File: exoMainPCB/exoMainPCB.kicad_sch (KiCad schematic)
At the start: 91 parts, among them J1 Conn_02x06_Odd_Even, J10 Conn_01x03_Pin, J11 USB_A, J12 USB_A, J13 USB_A, J14 Screw_Terminal_01x02, J2 HDMI_A, J3 USB_A, J4 Conn_01x02, J5 Conn_01x03, J6 Conn_01x03_Pin, J7 Conn_01x02, J8 Screw_Terminal_01x02, SW1 SW_SPDT, SW2 SW_Push, SW3 SW_SPDT, U1 MCP2515-I/ST, U14 SI8642ED-B-IS, U15 SN65HVD230D, U17 SM24CANB-02HTG, U2 MCP2515-I/ST, U3 BNO085, U4 SL2.1A, U5 MCP3008, U7 SN65HVD230D, U8 SM24CANB-02HTG, Y1 16 MHz, Y2 16 MHz, Y3 12 MHz, Y4 32.768 kHz

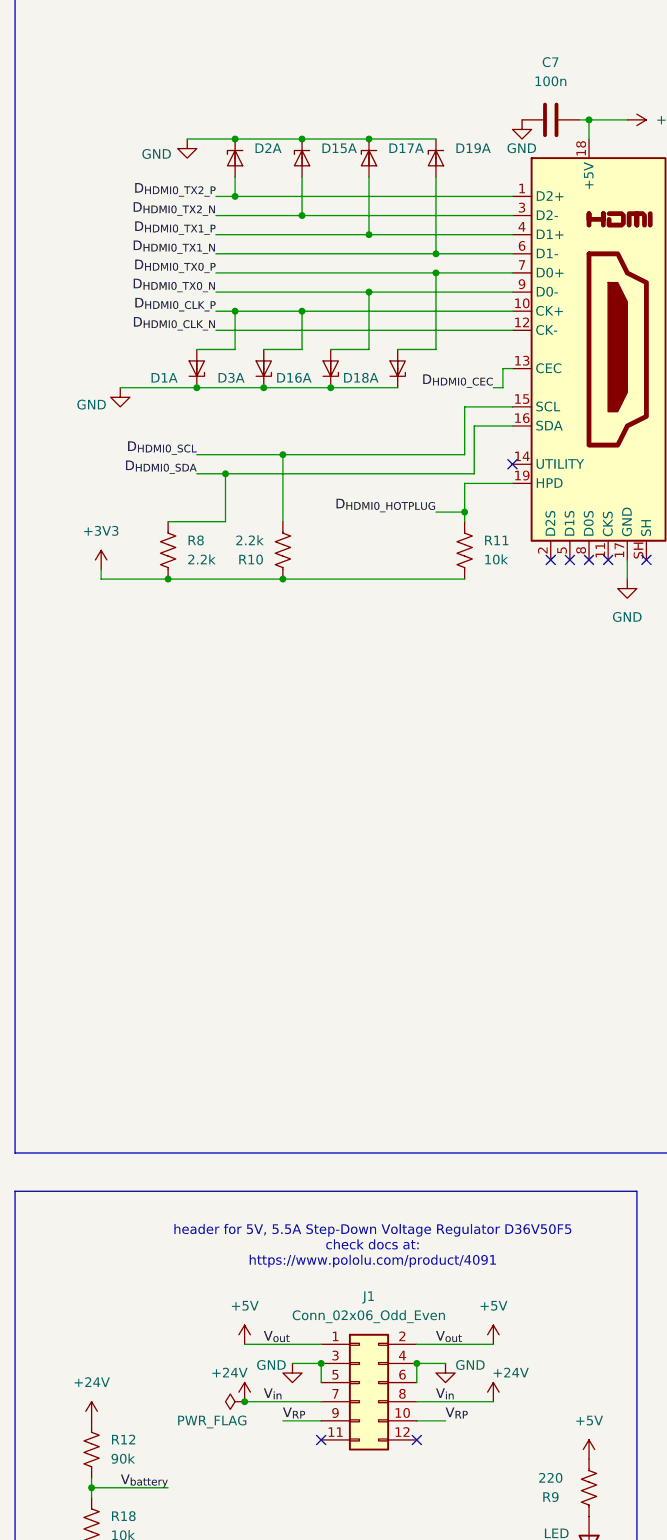
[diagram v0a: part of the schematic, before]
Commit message: fixed TVS diodes on HDMI, changed Vin and Vout to text rather than labels
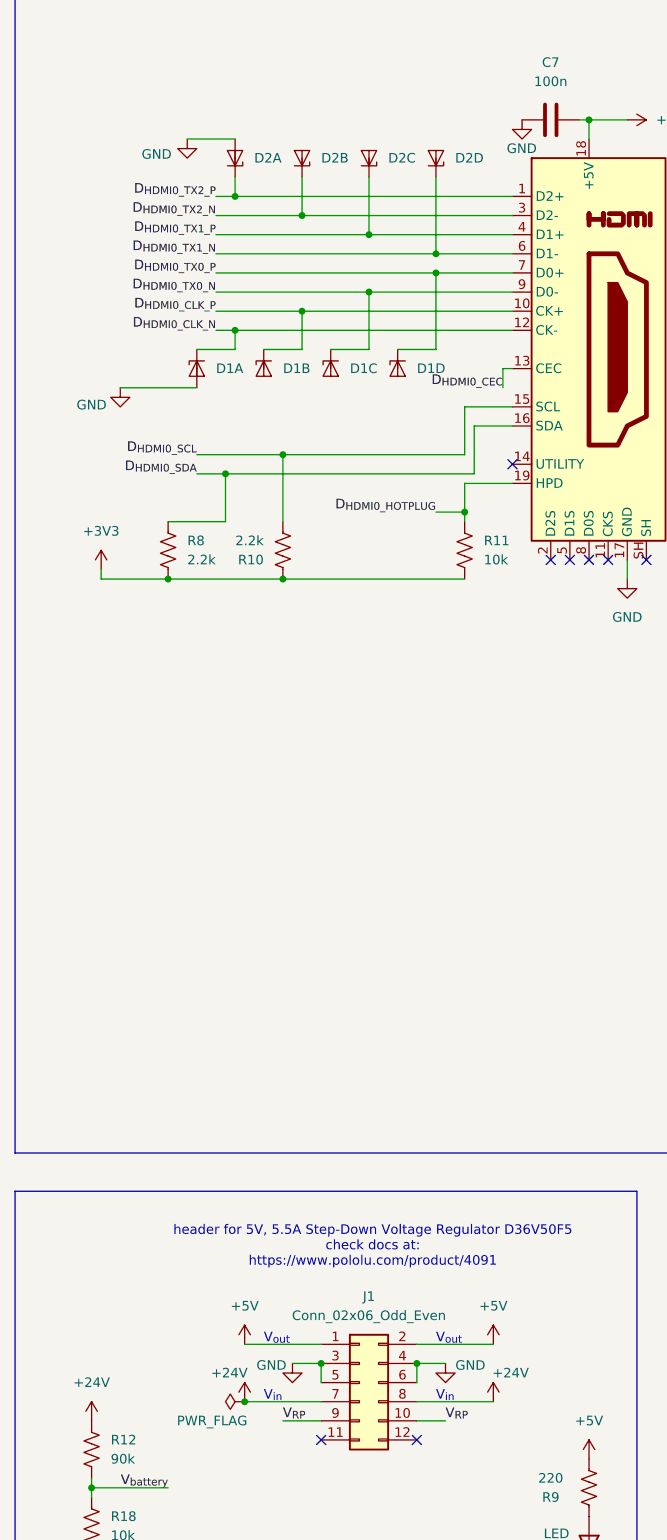
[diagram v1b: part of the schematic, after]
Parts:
- renumbered D18 to D1, D3 to D1, D16 to D1, D19 to D2, D15 to D2, D17 to D2
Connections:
- net D_{HDMI0_CLK_N}: now also D1.1 (K1)
- net D_{HDMI0_CLK_P}: now also D1.3 (K2); no longer D1.2 (A), D1.2 (A), D1.5 (A), D1.5 (A)
- net D_{HDMI0_TX0_N}: now also D1.4 (K3); no longer D1.2 (A), D1.5 (A)
- net D_{HDMI0_TX0_P}: now also D1.6 (K4); no longer D1.2 (A), D1.5 (A)
- net D_{HDMI0_TX1_N}: now also D2.6 (K4); no longer D2.2 (A), D2.5 (A)
- net D_{HDMI0_TX1_P}: now also D2.4 (K3); no longer D2.2 (A), D2.5 (A)
- net D_{HDMI0_TX2_N}: now also D2.3 (K2); no longer D2.2 (A), D2.5 (A)
- net D_{HDMI0_TX2_P}: now also D2.1 (K1); no longer D2.2 (A), D2.5 (A)
- net GND: now also D1.2 (A), D1.5 (A), D2.2 (A), D2.5 (A); no longer D1.1 (K1), D1.1 (K1), D1.1 (K1), D1.1 (K1), D2.1 (K1), D2.1 (K1), D2.1 (K1), D2.1 (K1)
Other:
- note added: "V_{in}"
- note added: "V_{out}"
- moved on the sheet: D1A, D2A

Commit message: assigned all footprints, created new footprints based on part availability
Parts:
- added C18, C20, C21, C22: 47uF, Capacitor_SMD:C_0805_2012Metric, symbol Device:C
- added J15: Conn_01x03, Connector_PinSocket_2.54mm:PinSocket_1x03_P2.54mm_Vertical, symbol Connector_Generic:Conn_01x03
- added J16: Conn_01x02, Connector_PinSocket_2.54mm:PinSocket_1x02_P2.54mm_Vertical, symbol Connector_Generic:Conn_01x02
- added J9: Conn_01x12, Connector_PinSocket_2.54mm:PinSocket_1x12_P2.54mm_Vertical, symbol Connector_Generic:Conn_01x12
- C1, C10, C11, C12, C15, C16, C17, C19, C2, C3, C33, C35, C4, C5, C6, C7: footprint (none) -> Capacitor_SMD:C_0805_2012Metric
- C13, C14, C8, C9: value 100uF -> 47uF; footprint (none) -> Capacitor_SMD:C_0805_2012Metric
- J1: footprint (none) -> Connector_PinSocket_2.54mm:PinSocket_2x06_P2.54mm_Vertical
- J10, J6: footprint (none) -> Connector_PinHeader_2.54mm:PinHeader_1x03_P2.54mm_Vertical
- J11, J12, J13, J3: footprint (none) -> BNO085:USB C2345
- J14, J8: footprint (none) -> BNO085:1x2 Screw Terminal C3703
- J2: footprint (none) -> Connector_Video:HDMI_A_Molex_208658-1001_Horizontal
- J4, J7: footprint (none) -> Connector_PinSocket_2.54mm:PinSocket_1x02_P2.54mm_Vertical
- J5: footprint (none) -> Connector_PinSocket_2.54mm:PinSocket_1x03_P2.54mm_Vertical
- JP1, JP2, JP7, JP8: footprint (none) -> Jumper:SolderJumper-2_P1.3mm_Open_RoundedPad1.0x1.5mm
- JP3, JP4, JP5, JP6, JP9: footprint (none) -> Jumper:SolderJumper-2_P1.3mm_Bridged_RoundedPad1.0x1.5mm
- R1, R10, R11, R12, R17, R18, R2, R3, R4, R5, R6, R7, R8: footprint (none) -> Resistor_SMD:R_0805_2012Metric
- R13, R14, R15, R16, R26, R9: footprint (none) -> Resistor_SMD:R_1206_3216Metric
- SW1, SW3: footprint (none) -> BNO085:ALPSALPINE C125042
- SW2: footprint (none) -> BNO085:SPEH SMD Pushbutton
- U1, U2: footprint SOP65P640X120-20N -> MCP2515-IST:SOP65P640X120-20N
- U14: footprint SOIC127P1030X265-16N -> SI8642ED-B-IS:SOIC127P1030X265-16N
- U15, U7: footprint SOIC127P600X175-8N -> SN65HVD230:SOIC127P600X175-8N
- U17, U8: footprint SM24CANB02HTG -> SM24CANB:SM24CANB02HTG
- U4: footprint my_lib:SOP-16_L10.0-W3.9-P1.27-LS6.0-BL -> Package_SO:SOP-16_3.9x9.9mm_P1.27mm
- U5: footprint (none) -> Package_SO:SOIC-16_3.9x9.9mm_P1.27mm
- Y1, Y2, Y3, Y4: footprint (none) -> Crystal:Crystal_SMD_2520-4Pin_2.5x2.0mm
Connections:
- net +5V: now also C18.1, C20.1, C21.1, C22.1
- net GND: now also C18.2, C20.2, C21.2, C22.2, J9.1 (Pin_1)
- net MISO: now also J15.2 (Pin_2)
- net MOSI: now also J15.1 (Pin_1)
- net SCK: now also J15.3 (Pin_3)
- net SCL: now also J16.2 (Pin_2)
- net SDA: now also J16.1 (Pin_1)
- net GPIO21: now reaches Module1.25 (GPIO21)
- net GPIO21: now also J9.12 (Pin_12)
- net GPIO20: now reaches Module1.27 (GPIO20)
- net GPIO20: now also J9.11 (Pin_11)
- net GPIO16: now reaches Module1.29 (GPIO16)
- net GPIO16: now also J9.10 (Pin_10)
- net GPIO12: now reaches Module1.31 (GPIO12)
- net GPIO12: now also J9.9 (Pin_9)
- net GPIO24: now reaches Module1.45 (GPIO24)
- net GPIO24: now also J9.8 (Pin_8)
- net GPIO23: now reaches Module1.47 (GPIO23)
- net GPIO23: now also J9.7 (Pin_7)
- net GPIO18: now reaches Module1.49 (GPIO18)
- net GPIO18: now also J9.6 (Pin_6)
- net GPIO15: now reaches Module1.51 (GPIO15)
- net GPIO15: now also J9.5 (Pin_5)
- net GPIO4: now reaches Module1.54 (GPIO4)
- net GPIO4: now also J9.3 (Pin_3)
- net GPIO14: now reaches Module1.55 (GPIO14)
- net GPIO14: now also J9.4 (Pin_4)
- new net +3.3V: J9.2 (Pin_2)
- no-connect marks 144 -> 134
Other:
- note added: "Extra Connection Pins for Future Modification"
- moved on the sheet: C13, C14, C8, C9

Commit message: pcb layout complete
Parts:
- removed JP6: SolderJumper_2_Bridged, Jumper:SolderJumper-2_P1.3mm_Bridged_RoundedPad1.0x1.5mm, symbol Jumper:SolderJumper_2_Bridged
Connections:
- net +24V: no longer J5.2 (Pin_2)
- net +3V3: no longer C16.2, U4.13 (VDD33)
- net +5V: now also Module1.77 (+5v_(Input)), Module1.79 (+5v_(Input)), Module1.81 (+5v_(Input)), Module1.83 (+5v_(Input)), Module1.85 (+5v_(Input)), Module1.87 (+5v_(Input))
- net D_{HDMI0_CLK_N}: now also D1.6 (K4); no longer D1.1 (K1)
- net D_{HDMI0_CLK_P}: now also D1.4 (K3); no longer D1.3 (K2)
- net D_{HDMI0_TX0_N}: now also D1.3 (K2); no longer D1.4 (K3)
- net D_{HDMI0_TX0_P}: now also D1.1 (K1); no longer D1.6 (K4)
- net V_{RP}: now also J5.2 (Pin_2)
- net +1V8: no longer names the net of C15.2, U4.14 (VDD18)
- net +1V8: no longer Module1.88 (+1.8v_(Output))
- new net: C16.2, U4.13 (VDD33)
- no-connect marks 134 -> 135

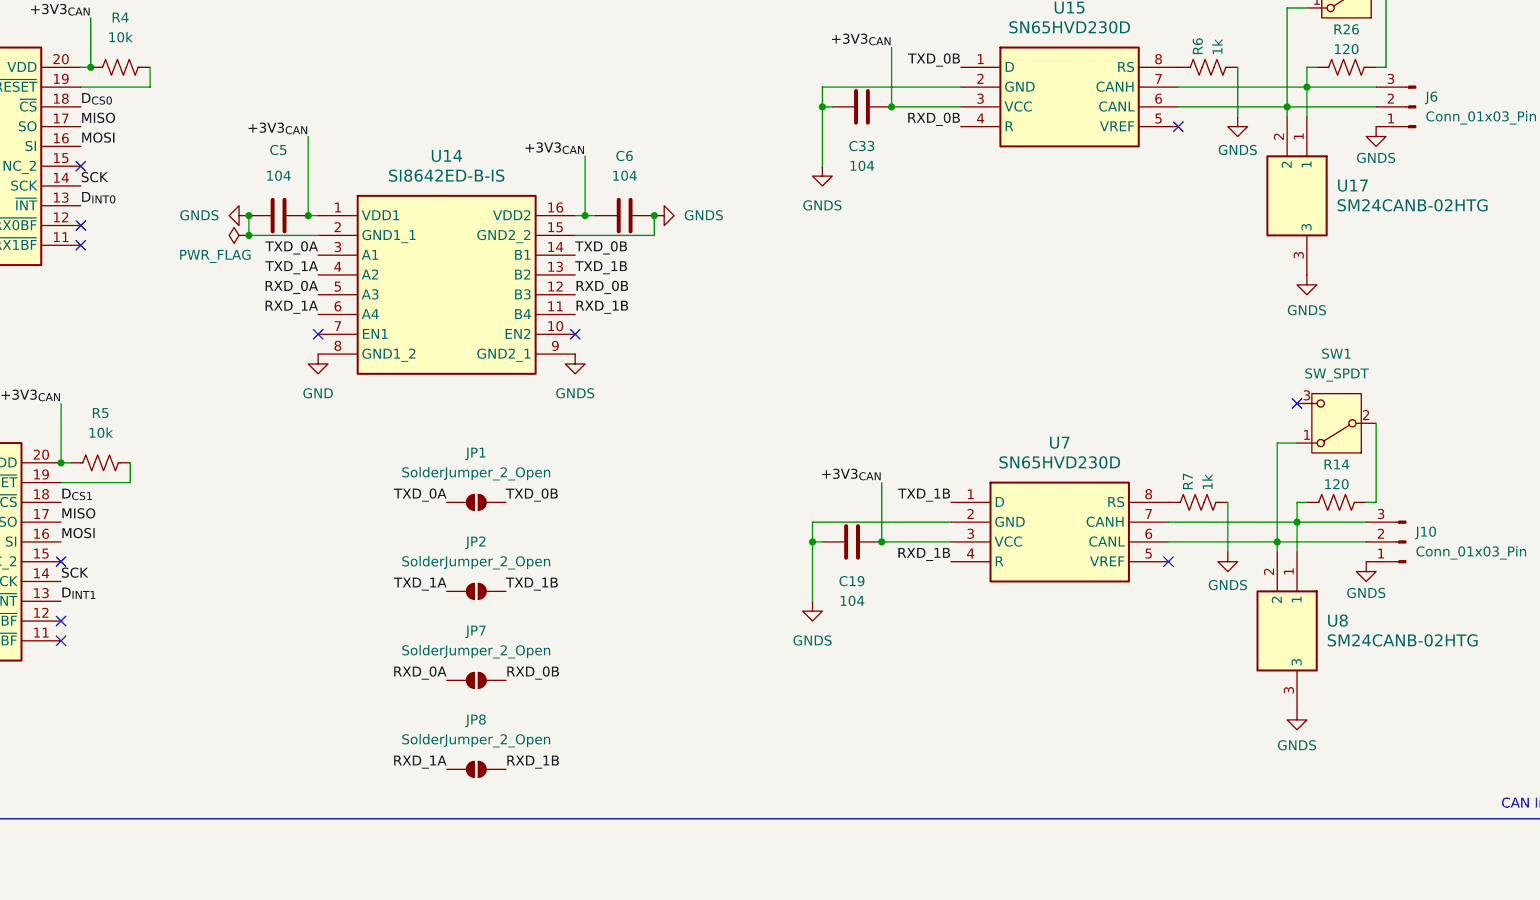
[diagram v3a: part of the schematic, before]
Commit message: added silkscreen labels, completed ground pours
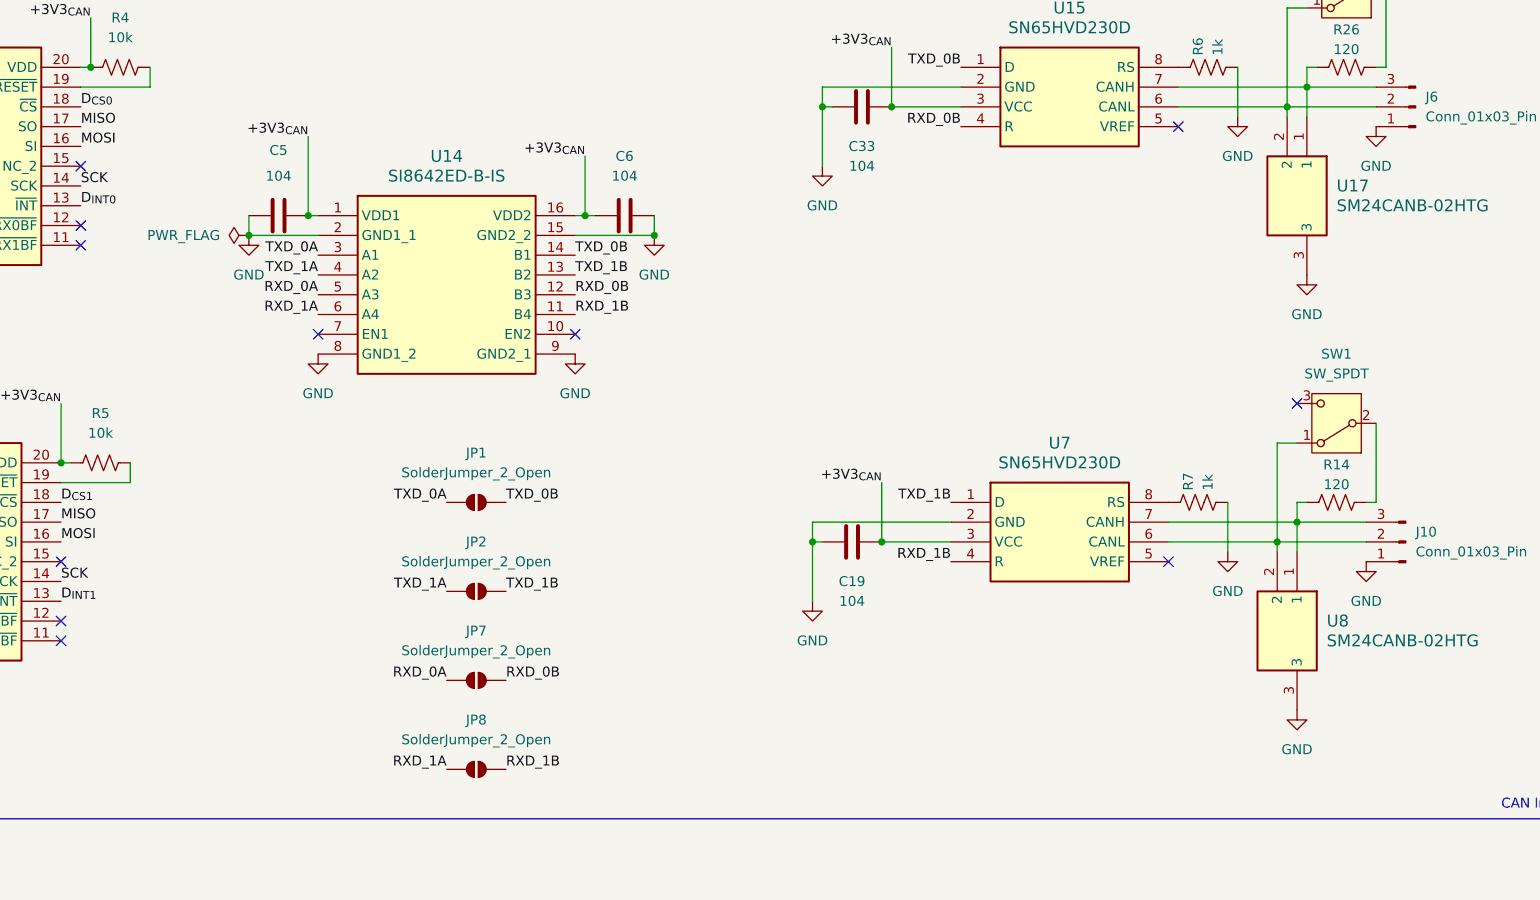
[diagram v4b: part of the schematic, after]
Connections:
- net GNDS is gone; now on net GND: C19.1, C33.1, C5.1, C6.2, J10.1 (Pin_1), J6.1 (Pin_1), R6.2, R7.2, U14.15 (GND2_2), U14.2 (GND1_1), U14.9 (GND2_1), U15.2 (GND), U17.3, U7.2 (GND), U8.3

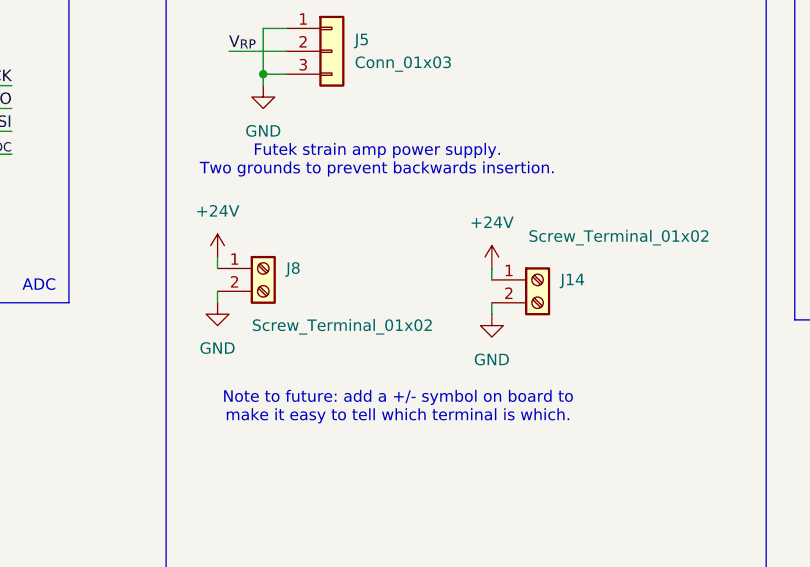
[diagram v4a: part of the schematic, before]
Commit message: added e stop screw terminal, corrected vias, traces, and pours
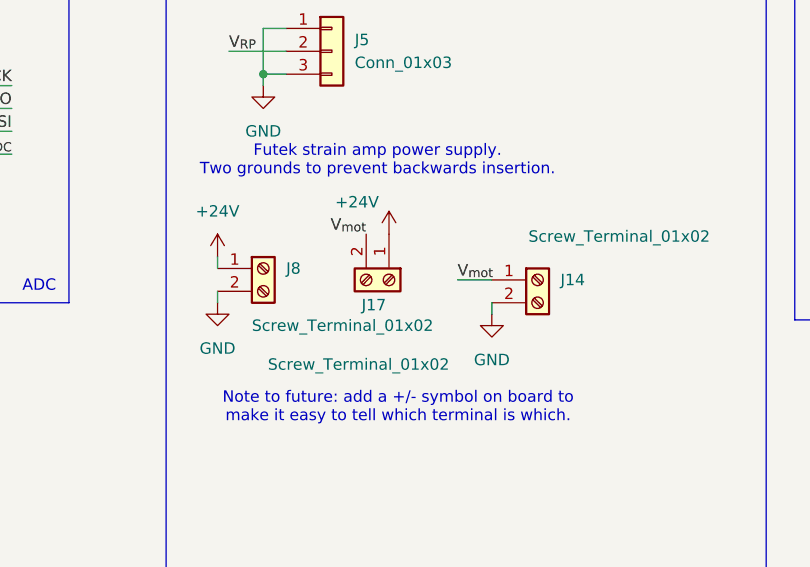
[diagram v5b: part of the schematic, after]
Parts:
- added J17: Screw_Terminal_01x02, BNO085:1x2 Screw Terminal C3703, symbol Connector:Screw_Terminal_01x02
- C1, C10, C11, C12, C13, C14, C15, C16, C17, C18, C19, C2, C20, C21, C22, C3, C33, C35, C4, C5, C6, C7, C8, C9: footprint Capacitor_SMD:C_0805_2012Metric -> Capacitor_SMD:C_0603_1608Metric
- R1, R10, R11, R12, R17, R18, R2, R3, R4, R5, R6, R7, R8: footprint Resistor_SMD:R_0805_2012Metric -> Resistor_SMD:R_0603_1608Metric
- R9: footprint Resistor_SMD:R_1206_3216Metric -> Resistor_SMD:R_0603_1608Metric
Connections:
- net +24V: now also J17.1 (Pin_1); no longer J14.1 (Pin_1)
- new net V_{mot}: J14.1 (Pin_1), J17.2 (Pin_2)

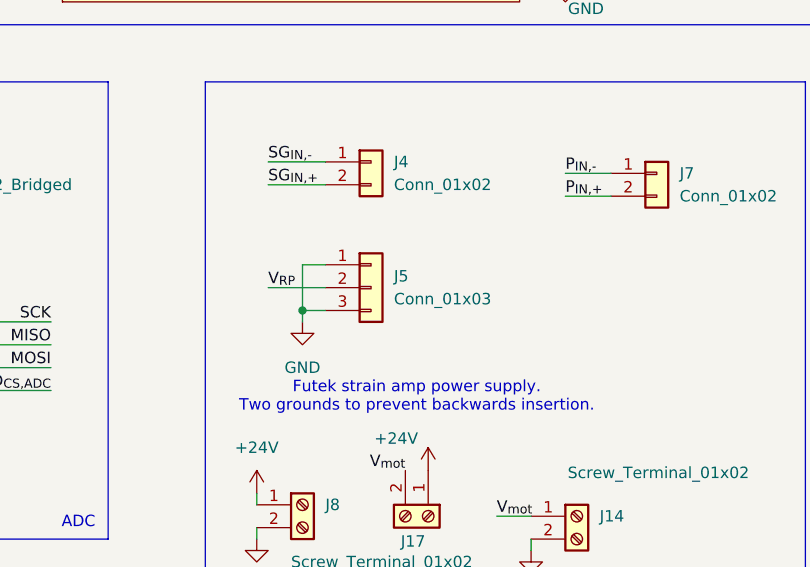
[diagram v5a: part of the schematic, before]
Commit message: FIXED condensed pcb layout, put stuff in the back, replaced headers with GH JST and power terminals with XT60
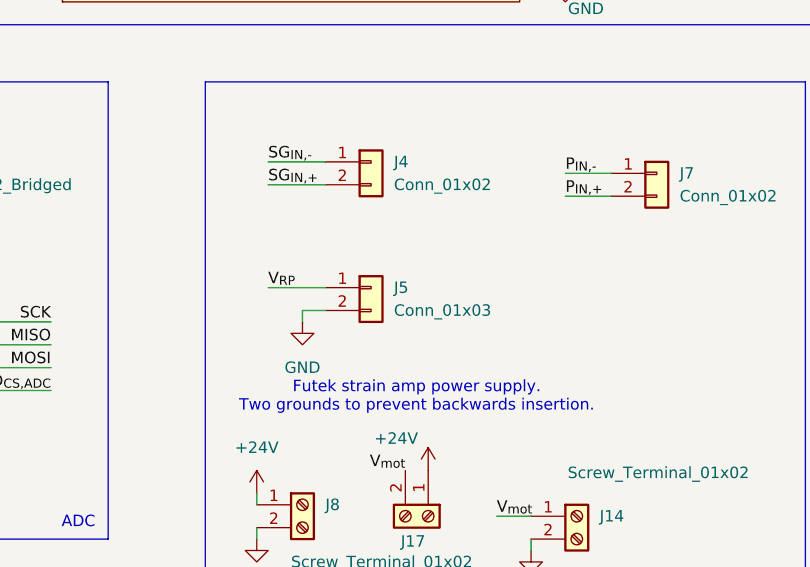
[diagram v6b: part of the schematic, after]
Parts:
- J5: symbol Connector_Generic:Conn_01x03 -> Connector_Generic:Conn_01x02
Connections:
- net GND: now also J5.2 (Pin_2); no longer J5.1 (Pin_1), J5.3 (Pin_3)
- net V_{RP}: now also J5.1 (Pin_1); no longer J5.2 (Pin_2)
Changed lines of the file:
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@@
 	)
 	(junction
-		(at 102.87 342.9)
-		(diameter 0)
-		(color 0 0 0 0)
-	)
-	(junction
 		(at 520.7 52.07)
 		(diameter 0)
@@
 	(wire
 		(pts
-			(xy 105.41 337.82) (xy 102.87 337.82)
-		)
-		(stroke
-			(width 0)
-			(type default)
-		)
-	)
-	(wire
-		(pts
 			(xy 167.64 45.72) (xy 167.64 90.17)
 		)
@@
 	(wire
 		(pts
-			(xy 102.87 337.82) (xy 102.87 342.9)
-		)
-		(stroke
-			(width 0)
-			(type default)
-		)
-	)
-	(wire
-		(pts
 			(xy 30.48 349.25) (xy 36.83 349.25)
 		)
@@
 	)
 	(symbol
-		(lib_id "Connector_Generic:Conn_01x03")
+		(lib_id "Connector_Generic:Conn_01x02")
 		(at 110.49 340.36 0)
 		(unit 1)
@@
 		(fields_autoplaced yes)
 		(property "Reference" "J5"
-			(at 113.03 339.0899 0)
+			(at 113.03 340.3599 0)
 			(effects
 				(font
@@
 		)
 		(property "Value" "Conn_01x03"
-			(at 113.03 341.6299 0)
+			(at 113.03 342.8999 0)
 			(effects
 				(font
@@
 			)
 		)
-		(property "Description" "Generic connector, single row, 01x03, script generated (kicad-library-utils/schlib/autogen/connector/)"
+		(property "Description" "Generic connector, single row, 01x02, script generated (kicad-library-utils/schlib/autogen/connector/)"
 			(at 110.49 340.36 0)
 			(effects
@@
 			)
 		)
-		(pin "3"
-		)
 		(pin "2"
